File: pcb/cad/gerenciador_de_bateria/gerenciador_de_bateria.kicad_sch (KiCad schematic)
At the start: 51 parts, among them J1 Conn_01x02_Male, J12 Conn_01x02_Male, J14 Conn_01x03_Male, J2 Conn_01x02_Male, J20 Conn_01x02_Male, J21 Conn_01x03_Male, J3 Conn_01x03_Male, J9 Conn_01x02_Male, SW1 SW_Push, U1 USB_BQ25629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

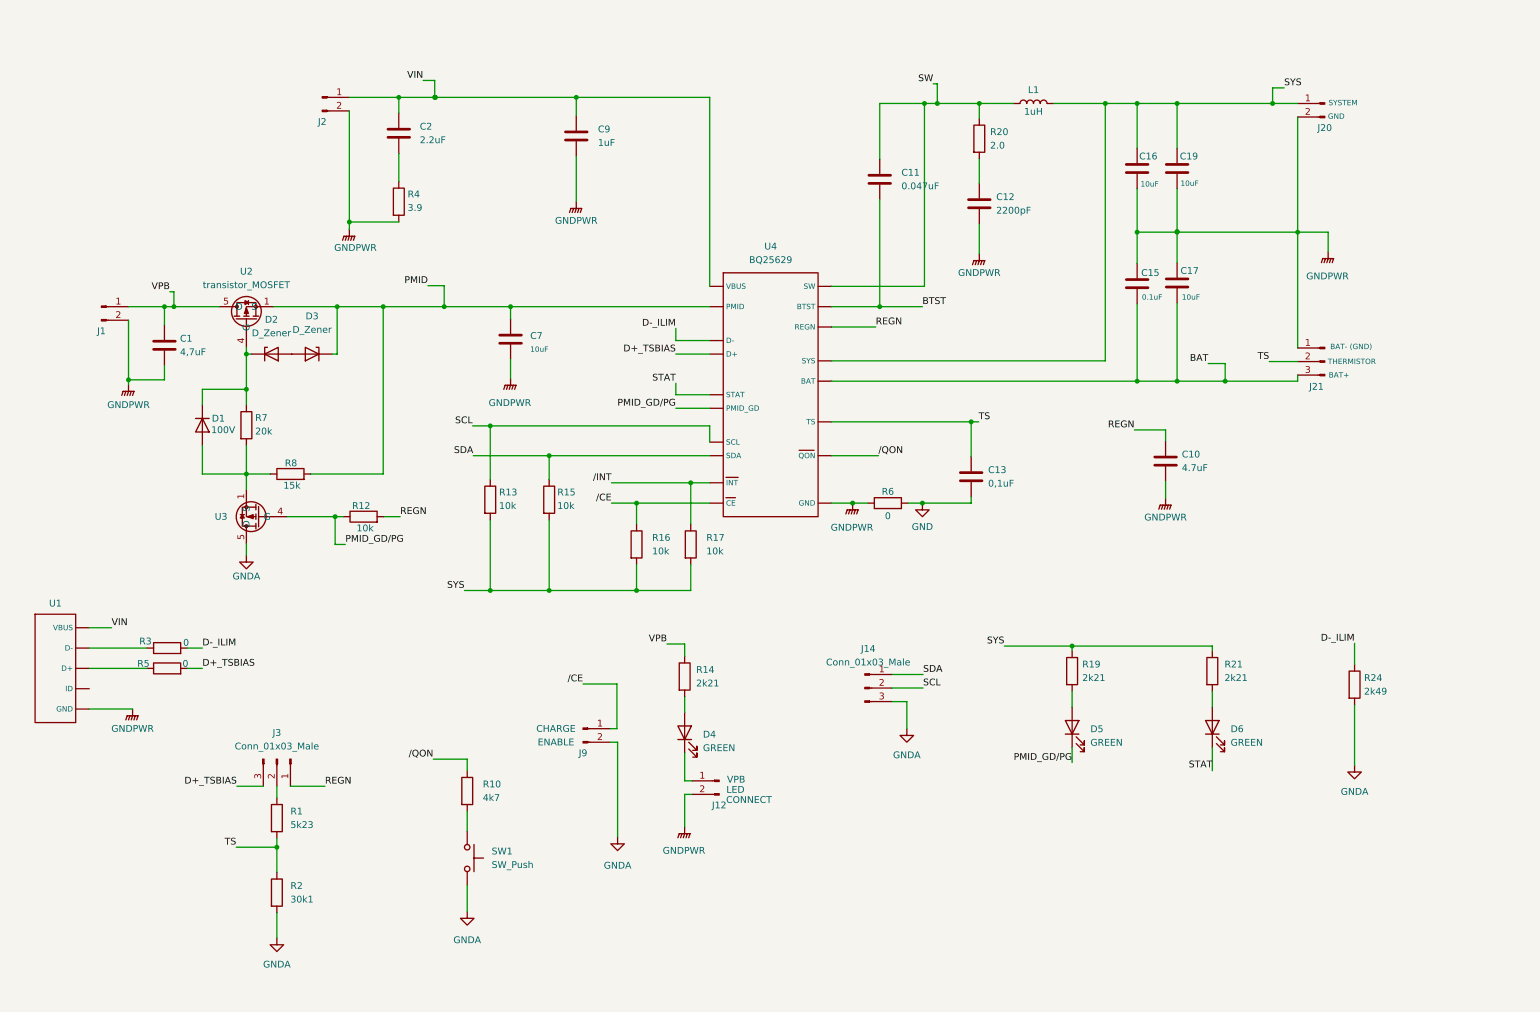
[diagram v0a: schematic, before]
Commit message: Otimização do esquemático do gerenciador_de_bateria, PCB atualizada com o USB centralizado no gerenciador_de_bateria_2.0, no gerenciador_de_bateria a PCB foi inicializada e finalizada
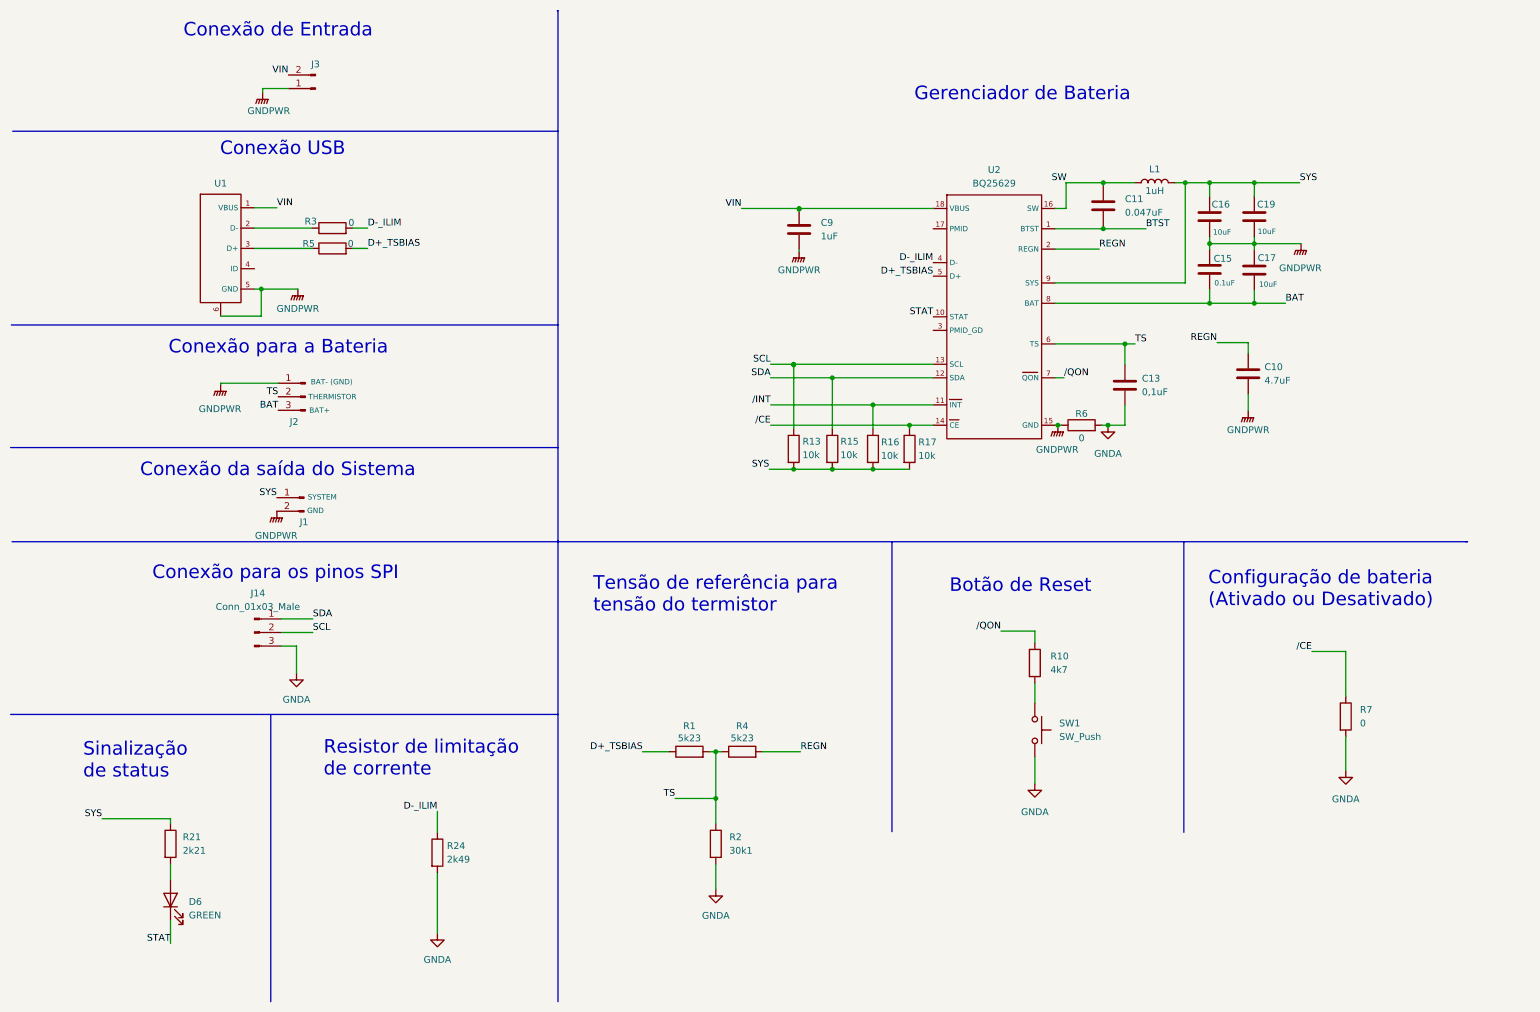
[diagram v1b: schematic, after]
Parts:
- removed C1: 4,7uF, Capacitor_SMD:C_0805_2012Metric, symbol Device:C
- removed C12: 2200pF, Capacitor_SMD:C_0805_2012Metric, symbol Device:C
- removed C2: 2.2uF, Capacitor_SMD:C_0805_2012Metric, symbol Device:C
- removed C7: 10uF, Capacitor_SMD:C_0805_2012Metric, symbol Device:C
- removed D1: 100V, Diode_SMD:D_0805_2012Metric, symbol Device:D
- removed D2, D3: D_Zener, Diode_SMD:D_0805_2012Metric, symbol Device:D_Zener
- removed D4, D5: GREEN, LED_SMD:LED_0805_2012Metric, symbol Device:LED
- removed J12, J2, J20, J9: Conn_01x02_Male, Connector_PinHeader_2.54mm:PinHeader_1x02_P2.54mm_Vertical, symbol Connector:Conn_01x02_Male
- removed J21, J3: Conn_01x03_Male, Connector_PinHeader_2.54mm:PinHeader_1x03_P2.54mm_Vertical, symbol Connector:Conn_01x03_Male
- removed R12: 10k, Resistor_SMD:R_0805_2012Metric, symbol Device:R
- removed R14, R19: 2k21, Resistor_SMD:R_0805_2012Metric, symbol Device:R
- removed R20: 2.0, Resistor_SMD:R_0805_2012Metric, symbol Device:R
- removed R8: 15k, Resistor_SMD:R_0805_2012Metric, symbol Device:R
- removed U2, U3: transistor_MOSFET, symbol gerenciador_de_bateria_simbolos:transistor_MOSFET
- removed U4: BQ25629, gerenciador_de_bateria_fp:WQFN-HR18_RYK_TEX, symbol gerenciador_de_bateria_simbolos:BQ25629
- added J2: Conn_01x03_Male, Connector_PinHeader_2.54mm:PinHeader_1x03_P2.54mm_Vertical, symbol Connector:Conn_01x03_Male
- added J3: Conn_01x02_Male, Connector_PinHeader_2.54mm:PinHeader_1x02_P2.54mm_Vertical, symbol Connector:Conn_01x02_Male
- added U2: BQ25629, gerenciador_de_bateria_fp:WQFN-HR18_RYK_TEX, symbol gerenciador_de_bateria_simbolos:BQ25629
- J1: Campo4 (none) -> SYSTEM; GND (none) -> GND
- L1: footprint Inductor_SMD:L_0805_2012Metric -> Inductor_SMD:L_1210_3225Metric
- R4: value 3.9 -> 5k23
- R7: value 20k -> 0
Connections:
- net GND is gone; now on net GNDA: C13.2, R6.2
- net VPB is gone; now on net SYS: J1.1 (Pin_1)
- net BAT: now also J2.3 (Pin_3), U2.8 (BAT)
- net BTST: now also U2.1 (BTST)
- net D+_TSBIAS: now also R1.1, U2.5 (D+)
- net D-_ILIM: now also U2.4 (D-)
- net GNDA: now also R7.2
- net GNDPWR: now also U1.5 (GND), U1.6, J2.1 (Pin_1), J3.1 (Pin_1), U2.15 (GND); no longer R4.2, U1. (VBUS)
- net REGN: now also R4.2, U2.2 (REGN)
- net SCL: now also U2.13 (SCL)
- net SDA: now also U2.12 (SDA)
- net STAT: now also U2.10 (STAT)
- net SW: now also U2.16 (SW)
- net SYS: now also U2.9 (SYS)
- net TS: now also R4.1, J2.2 (Pin_2), U2.6 (TS)
- net VIN: now also U1.1 (VBUS), J3.2 (Pin_2), U2.18 (VBUS); no longer U1. (VBUS)
- net /CE: now also R17.1, R7.1, U2.14 (CE); no longer R16.1
- net /INT: now also R16.1, U2.11 (INT); no longer R17.1
- net /QON: now also U2.7 (QON)
- net at R5.1: now also U1.3 (D+); no longer U1. (VBUS)
- net at R3.1: now also U1.2 (D-); no longer U1. (VBUS)
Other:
- note added: "Botão de Reset"
- note added: "Conexão USB"
- note added: "Conexão da saída do Sistema"
- note added: "Conexão de Entrada"
- note added: "Conexão para a Bateria"
- note added: "Conexão para os pinos SPI"
- note added: "Configuração de bateria (Ativado ou Desativado)"
- note added: "Gerenciador de Bateria"
- note added: "Resistor de limitação de corrente"
- note added: "Sinalização de status"
- note added: "Tensão de referência para tensão do termistor"
- moved on the sheet: C10, C11, C13, C15, C16, C17, C19, C9, D6, J14, L1, R10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
